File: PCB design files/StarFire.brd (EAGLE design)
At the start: 43.7 x 43.8 mm, 29 parts, among them U2 ATTINY85-20SU

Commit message: cleanup and sort
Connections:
- net N$13: now also U$1.+$2
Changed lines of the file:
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@@
 <?xml version="1.0" encoding="utf-8"?>
 <!DOCTYPE eagle SYSTEM "eagle.dtd">
-<eagle version="7.5.0">
+<eagle version="7.2.0">
 <drawing>
 <settings>
@@
 <wire x1="22.5425" y1="17.78" x2="22.5314" y2="17.657809375" width="0.254" layer="16"/>
 <wire x1="23.8125" y1="31.115" x2="24.0127875" y2="31.30850625" width="0.254" layer="16"/>
+<contactref element="U$1" pad="+$2"/>
+<wire x1="12.416234375" y1="19.711953125" x2="22.5425" y2="17.78" width="0" layer="19" extent="16-16"/>
 </signal>
 <signal name="GND">

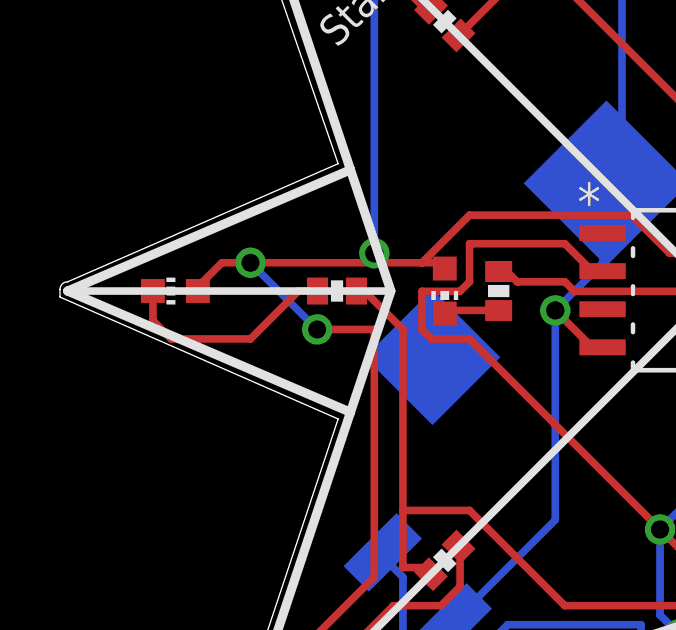
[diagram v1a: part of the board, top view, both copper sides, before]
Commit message: Fixed routing errors
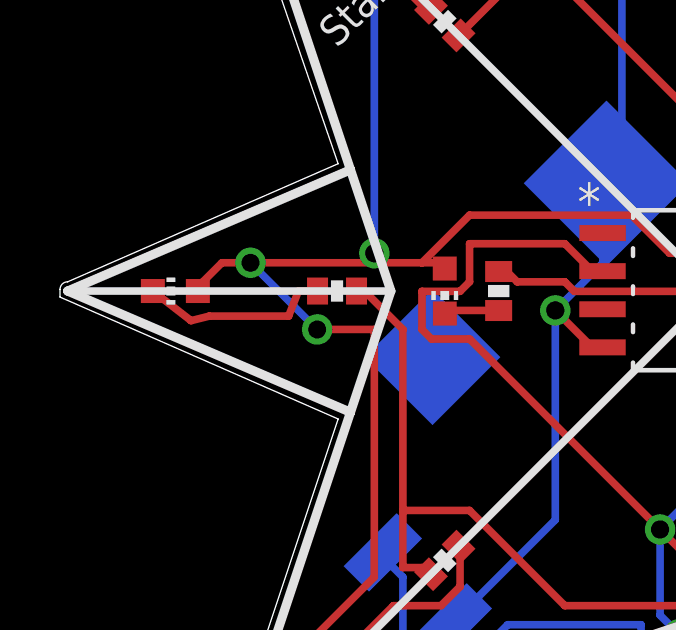
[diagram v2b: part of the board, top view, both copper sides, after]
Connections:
- net N$13: no longer U$1.+$2
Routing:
- net N$4: track 7.39 -> 6.42 mm
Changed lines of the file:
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@@
 <contactref element="R4" pad="1"/>
 <wire x1="3.0961" y1="21.918128125" x2="3.0988" y2="21.915428125" width="0.254" layer="1"/>
-<wire x1="3.0988" y1="21.915428125" x2="3.0988" y2="20.9296" width="0.254" layer="1"/>
-<wire x1="3.0988" y1="20.9296" x2="3.7084" y2="20.32" width="0.254" layer="1"/>
-<wire x1="3.7084" y1="20.32" x2="6.35" y2="20.32" width="0.254" layer="1"/>
-<wire x1="6.35" y1="20.32" x2="7.948128125" y2="21.918128125" width="0.254" layer="1"/>
+<wire x1="3.0988" y1="21.915428125" x2="4.3688" y2="20.9296" width="0.254" layer="1"/>
+<wire x1="4.3688" y1="20.9296" x2="4.9784" y2="21.082" width="0.254" layer="1"/>
+<wire x1="4.9784" y1="21.082" x2="7.62" y2="21.082" width="0.254" layer="1"/>
+<wire x1="7.62" y1="21.082" x2="7.948128125" y2="21.918128125" width="0.254" layer="1"/>
 <wire x1="7.948128125" y1="21.918128125" x2="8.584253125" y2="21.918128125" width="0.254" layer="1"/>
 </signal>
@@
 <wire x1="22.5425" y1="17.78" x2="22.5314" y2="17.657809375" width="0.254" layer="16"/>
 <wire x1="23.8125" y1="31.115" x2="24.0127875" y2="31.30850625" width="0.254" layer="16"/>
-<contactref element="U$1" pad="+$2"/>
-<wire x1="12.416234375" y1="19.711953125" x2="22.5425" y2="17.78" width="0" layer="19" extent="16-16"/>
 </signal>
 <signal name="GND">
